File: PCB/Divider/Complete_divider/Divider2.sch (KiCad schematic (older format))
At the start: 29 parts

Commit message: Reorganize
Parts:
- removed R? (x2): 10M, Resistor_SMD:R_1206_3216Metric, symbol Device:R
- added E31, E32, E33, E34, E35, E36, E37, E38, E39, E40, E41, E42, E43, E44, E45, E46, E47, E48, E49, E50, E51, E52, E53, E54, E55, E56, E57: Electr., Connector:Pad_for_electrode, symbol Connector:Conn_01x01_Female
- added J31, J58: Electr., Connector_Pin:Pin_D1.0mm_L10.0mm, symbol Connector:Conn_01x01_Female
- gave numbers to parts that had none: 27
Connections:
- net APGRID: now also J58.1 (Pin_1)
- net DRIFTTUBE: now also R32.2, E31.1 (Pin_1), J31.1 (Pin_1)
- net at R32.1, R33.1: now also E32.1 (Pin_1)
- net at R33.2, R34.2: now also E33.1 (Pin_1)
- net at R34.1, R35.1: now also E34.1 (Pin_1)
- net at R35.2, R36.2: now also E35.1 (Pin_1)
- net at R36.1, R37.1: now also E36.1 (Pin_1)
- net at R38.1, R39.1: now also E38.1 (Pin_1)
- net at R37.2, R38.2: now also E37.1 (Pin_1)
- net at R39.2, R40.2: now also E39.1 (Pin_1)
- net at R40.1, R41.1: now also E40.1 (Pin_1)
- net at R41.2, R42.2: now also E41.1 (Pin_1)
- net at R42.1, R43.1: now also E42.1 (Pin_1)
- net at R44.1, R45.1: now also E44.1 (Pin_1)
- net at R43.2, R44.2: now also E43.1 (Pin_1)
- net at R45.2, R46.2: now also E45.1 (Pin_1)
- net at R46.1, R47.1: now also E46.1 (Pin_1)
- net at R47.2, R48.2: now also E47.1 (Pin_1)
- net at R48.1, R49.1: now also E48.1 (Pin_1)
- net at R50.1, R51.1: now also E50.1 (Pin_1)
- net at R49.2, R50.2: now also E49.1 (Pin_1)
- net at R51.2, R52.2: now also E51.1 (Pin_1)
- net at R52.1, R53.1: now also E52.1 (Pin_1)
- net at R53.2, R54.2: now also E53.1 (Pin_1)
- net at R54.1, R55.1: now also E54.1 (Pin_1)
- net at R56.1, R57.1: now also E56.1 (Pin_1)
- net at R55.2, R56.2: now also E55.1 (Pin_1)
- net at R57.2, R58.2: now also E57.1 (Pin_1)
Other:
- note added: "Annotation begins at 30\n28 Resistors\n27 electrodes\n\n"
- note added: "Only a pin not electrode"

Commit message: Most parts completed
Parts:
- renumbered J58 to E58, R32 to R31, R33 to R32, R34 to R33, R35 to R34, R36 to R35, R37 to R36, R38 to R37, R39 to R38, R40 to R39, R41 to R40, R42 to R41, R43 to R42, R44 to R43, R45 to R44, R46 to R45, R47 to R46, R48 to R47, R49 to R48, R50 to R49, R51 to R50, R52 to R51, R53 to R52, R54 to R53, R55 to R54, R56 to R55, R57 to R56, R58 to R57

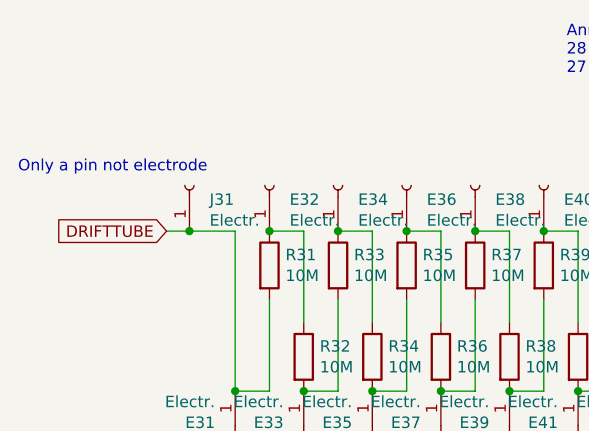
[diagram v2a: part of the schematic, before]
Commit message: Implementation of the HV sources footprints and schems
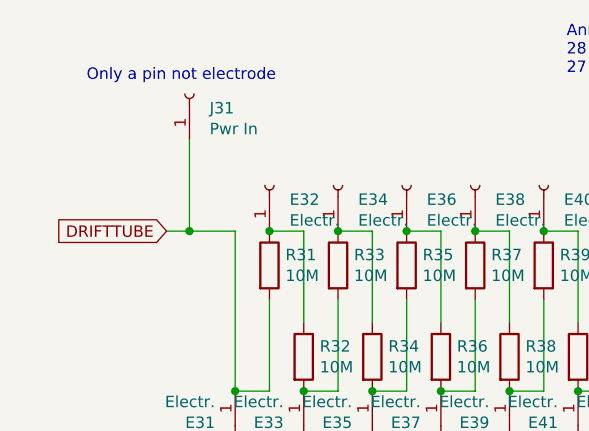
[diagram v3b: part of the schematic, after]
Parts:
- J31: value Electr. -> Pwr In
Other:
- moved on the sheet: J31
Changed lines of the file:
@@
 L Connector:Conn_01x01_Female J?
 U 1 1 5E7464A5
-P 3600 3300
+P 3600 2900
 AR Path="/5E6FA86A/5E7464A5" Ref="J?"  Part="1"
 AR Path="/5E63EFA9/5E7464A5" Ref="J31"  Part="1"
 AR Path="/5E7464A5" Ref="J31"  Part="1"
-F 0 "J31" V 3538 3212 50  0000 R CNN
-F 1 "Electr." V 3447 3212 50  0000 R CNN
-F 2 "Connector_Pin:Pin_D1.0mm_L10.0mm" H 3600 3300 50  0001 C CNN
-F 3 "~" H 3600 3300 50  0001 C CNN
-	1    3600 3300
+F 0 "J31" V 3538 2812 50  0000 R CNN
+F 1 "Pwr In" V 3447 2812 50  0000 R CNN
+F 2 "Connector_Pin:Pin_D1.0mm_L10.0mm" H 3600 2900 50  0001 C CNN
+F 3 "~" H 3600 2900 50  0001 C CNN
+	1    3600 2900
 	0    -1   -1   0
 $EndComp
@@
 Wire Wire Line
 	3800 3500 3800 4200
-Text Notes 2850 3250 0    50   ~ 0
+Text Notes 3150 2850 0    50   ~ 0
 Only a pin not electrode
 $Comp
@@
 $EndComp
 Connection ~ 3800 4200
+Wire Wire Line
+	3600 3100 3600 3500
 $EndSCHEMATC

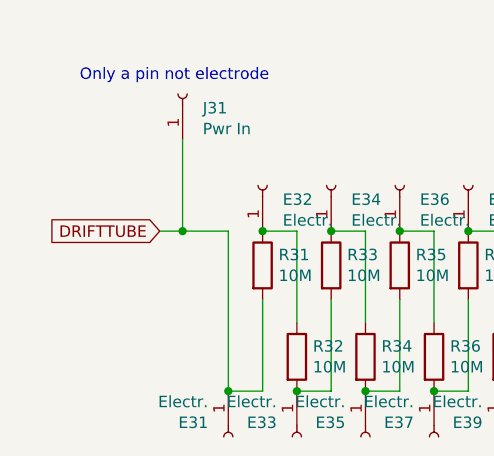
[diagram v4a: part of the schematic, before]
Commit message: Voltage measure circuits
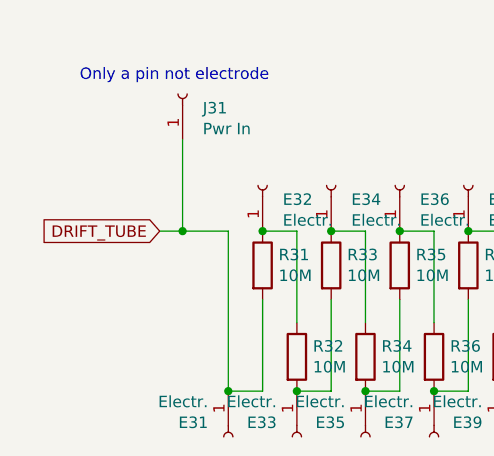
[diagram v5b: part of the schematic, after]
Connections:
- net DRIFTTUBE renamed DRIFT_TUBE
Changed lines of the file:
@@
 $Descr A4 11693 8268
 encoding utf-8
-Sheet 2 4
+Sheet 2 5
 Title ""
 Date ""
@@
 $EndComp
 Text GLabel 3500 3500 0    50   Input ~ 0
-DRIFTTUBE
+DRIFT_TUBE
 Text GLabel 8250 3500 2    50   Output ~ 0
 APGRID

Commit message: Begin PCB design
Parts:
- renumbered E32 to E1, E50 to E10, E52 to E11, E54 to E12, E56 to E13, E58 to E14, E31 to E15, E33 to E16, E35 to E17, E37 to E18, E39 to E19, E34 to E2, E41 to E20, E43 to E21, E45 to E22, E47 to E23, E49 to E24, E51 to E25, E53 to E26, E55 to E27, E57 to E28, E36 to E3, E38 to E4, E40 to E5, E42 to E6, E44 to E7, E46 to E8, E48 to E9, J31 to J1, R31 to R1, R49 to R10, R51 to R11, R53 to R12, R55 to R13, R57 to R14, R32 to R15, R34 to R16, R36 to R17, R38 to R18, R40 to R19, R33 to R2, R42 to R20, R44 to R21, R46 to R22, R48 to R23, R50 to R24, R52 to R25, R54 to R26, R56 to R27, R35 to R3, R37 to R4, R39 to R5, R41 to R6, R43 to R7, R45 to R8, R47 to R9

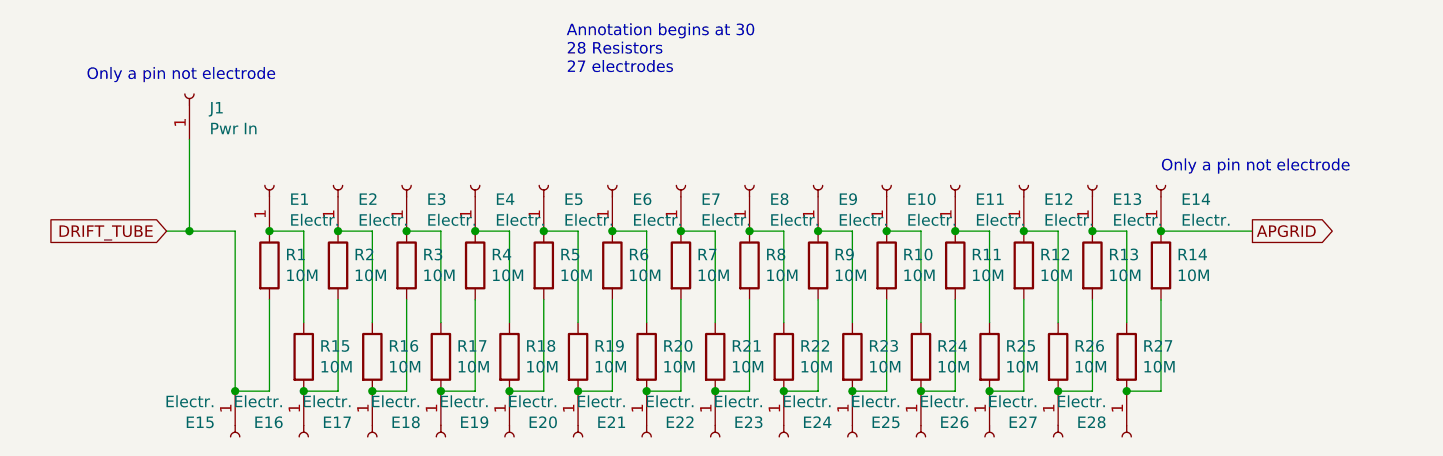
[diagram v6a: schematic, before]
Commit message: Updates of dividers 1 & 2
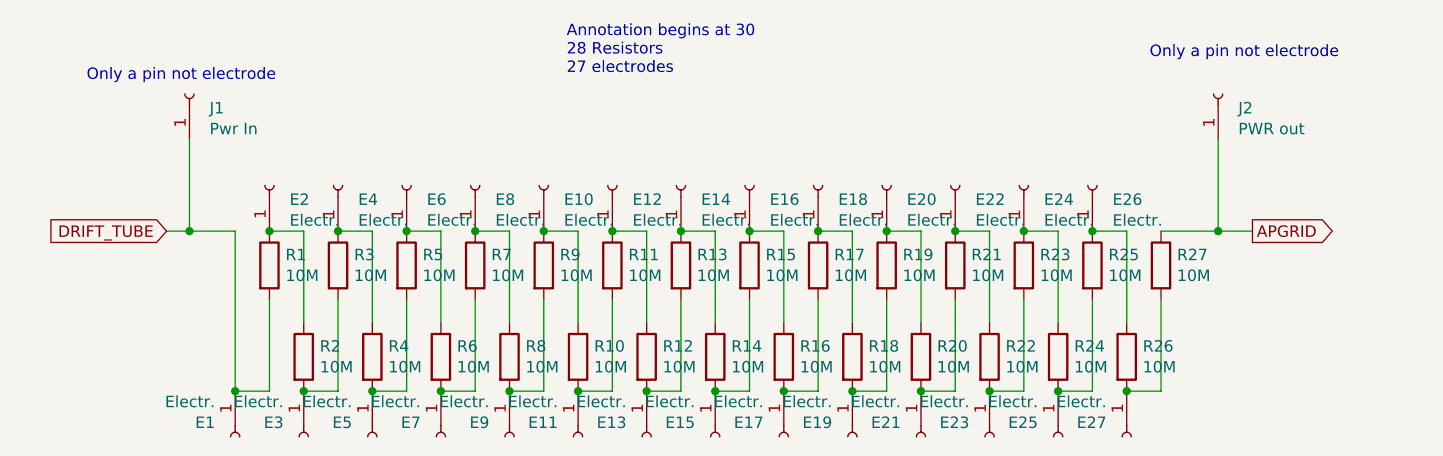
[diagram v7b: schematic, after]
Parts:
- J2: renamed from E14; value Electr. -> PWR out
- renumbered E15 to E1, E5 to E10, E20 to E11, E6 to E12, E21 to E13, E7 to E14, E22 to E15, E8 to E16, E23 to E17, E9 to E18, E24 to E19, E1 to E2, E10 to E20, E25 to E21, E11 to E22, E26 to E23, E12 to E24, E27 to E25, E13 to E26, E28 to E27, E16 to E3, E2 to E4, E17 to E5, E3 to E6, E18 to E7, E4 to E8, E19 to E9, R19 to R10, R6 to R11, R20 to R12, R7 to R13, R21 to R14, R8 to R15, R22 to R16, R9 to R17, R23 to R18, R10 to R19, R15 to R2, R24 to R20, R11 to R21, R25 to R22, R12 to R23, R26 to R24, R13 to R25, R27 to R26, R14 to R27, R2 to R3, R16 to R4, R3 to R5, R17 to R6, R4 to R7, R18 to R8, R5 to R9
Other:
- moved on the sheet: J2
